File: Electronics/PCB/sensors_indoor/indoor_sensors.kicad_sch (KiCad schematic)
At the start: 11 parts, among them J3 B5B-ZR, U2 SHT45-AD1F, U3 SCD41-D-R2, U4 SGP41, U5 LPS22DF, U6 TSOP38436, U8 SPS30, U9 OPT4001DTSR

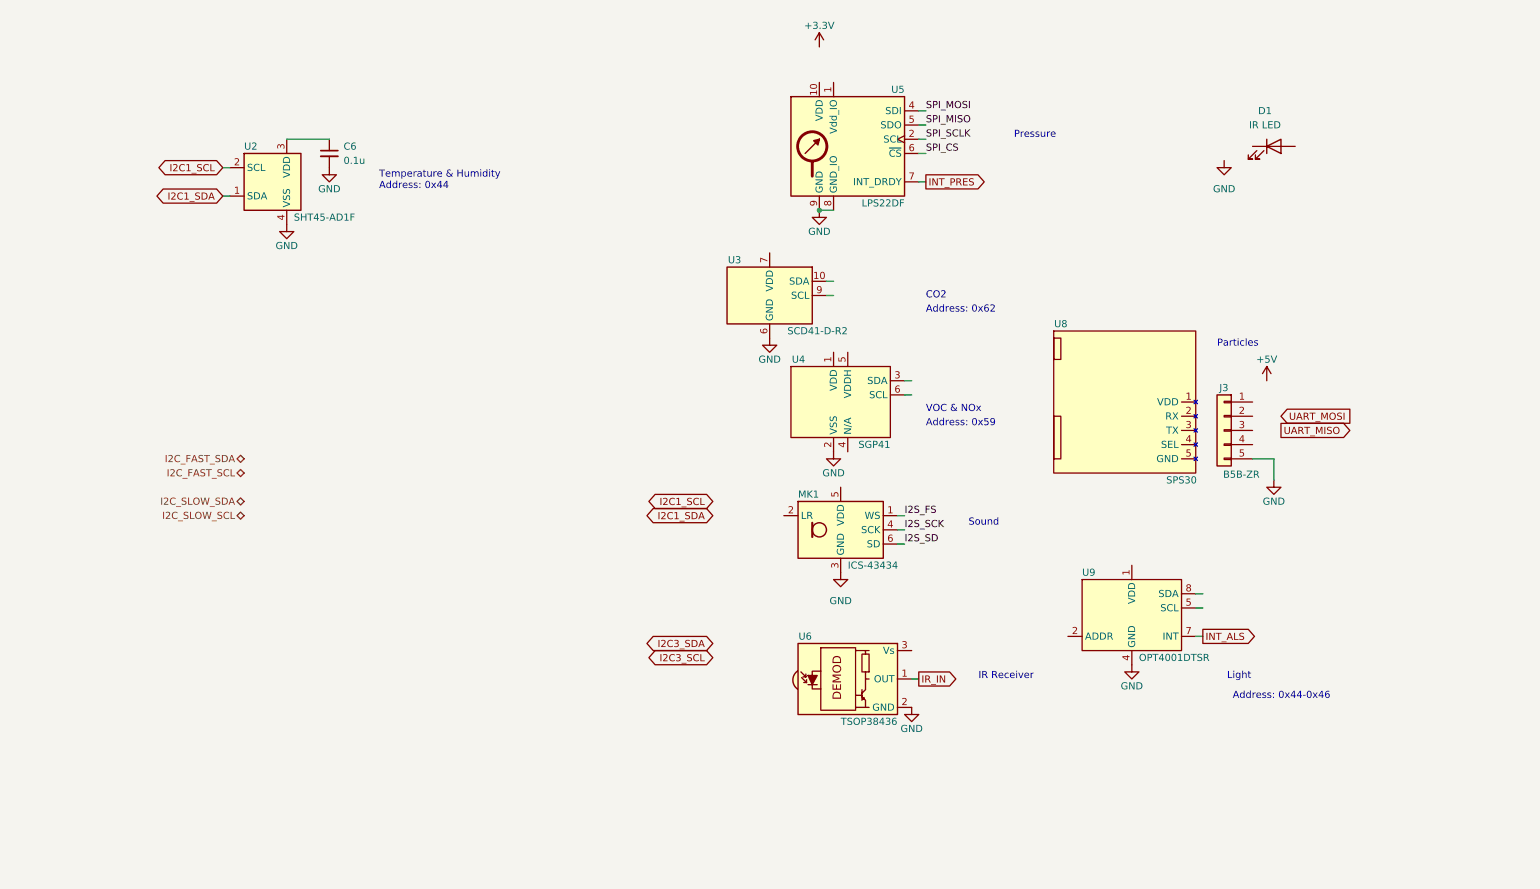
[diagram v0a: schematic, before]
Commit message: Added mounting holes and power supply
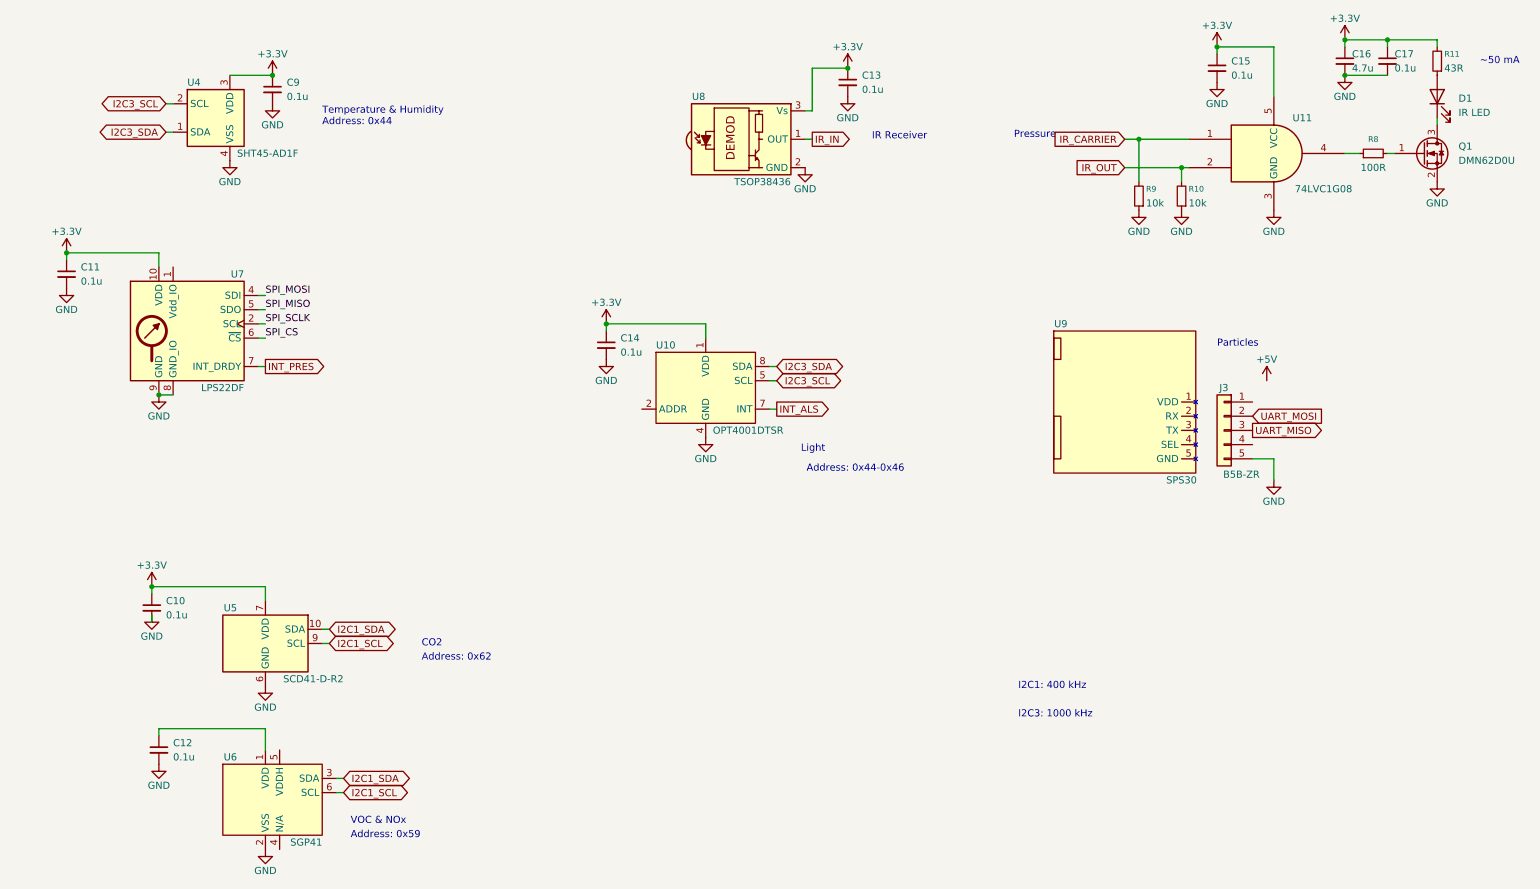
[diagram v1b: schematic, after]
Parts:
- removed MK1: ICS-43434, Sensor_Audio:InvenSense_ICS-43434-6_3.5x2.65mm, symbol Sensor_Audio:ICS-43434
- added C10, C11, C12, C13, C14, C15, C17: 0.1u, Capacitor_SMD:C_0402_1005Metric, symbol Device:C_Small
- added C16: 4.7u, Capacitor_SMD:C_0805_2012Metric, symbol Device:C_Small
- added Q1: DMN62D0U, Package_TO_SOT_SMD:SOT-23, symbol Transistor_FET:Q_NMOS_GSD
- added R10, R9: 10k, Resistor_SMD:R_0603_1608Metric, symbol Device:R_Small
- added R11: 43R, Resistor_SMD:R_0805_2012Metric, symbol Device:R_Small
- added R8: 100R, Resistor_SMD:R_0603_1608Metric, symbol Device:R_Small
- added U11: 74LVC1G08, Package_TO_SOT_SMD:SOT-23-5, symbol 74xGxx:74LVC1G08
- C9: renamed from C6; footprint (none) -> Capacitor_SMD:C_0402_1005Metric
- J3: MPN (none) -> B5B-ZR(LF)(SN); Mouser PN (none) -> 306-B5BZRLFSNP
- renumbered U9 to U10, U2 to U4, U3 to U5, U4 to U6, U5 to U7, U6 to U8, U8 to U9
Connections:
- net +3.3V: now also C9.1, U10.1 (VDD), U4.3 (VDD), U5.19 (VDD), U5.7 (VDD), U7.10 (VDD), U8.3 (Vs), C10.1, C11.1, C13.1, C14.1, C15.1, C16.1, C17.1, R11.2, U11.5 (VCC)
- net GND: now also C10.2, C11.2, C12.2, C13.2, C14.2, C15.2, C16.2, C17.2, Q1.2 (S), R10.1, R9.1, U11.3 (GND)
- net I2C1_SCL: now also U5.9 (SCL), U6.6 (SCL); no longer U4.2 (SCL)
- net I2C1_SDA: now also U5.10 (SDA), U6.3 (SDA); no longer U4.1 (SDA)
- net I2C3_SCL: now also U10.5 (SCL), U4.2 (SCL)
- net I2C3_SDA: now also U10.8 (SDA), U4.1 (SDA)
- net UART_MISO: now also J3.3 (Pin_3)
- net UART_MOSI: now also J3.2 (Pin_2)
- net at D1.1 (K): now also Q1.3 (D)
- net at D1.2 (A): now also R11.1
- net at U6.1 (VDD): now also C12.1
- new net: R8.1, U11.4
- new net: Q1.1 (G), R8.2
- new net IR_CARRIER: R9.2, U11.1
- new net IR_OUT: R10.2, U11.2
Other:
- note added: "I2C1: 400 kHz"
- note added: "I2C3: 1000 kHz"
- note added: "~50 mA"
- note removed: "Sound"
- moved on the sheet: C9, D1, U10, U4, U5, U6, U7, U8

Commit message: Swapped sides of everything and started routing
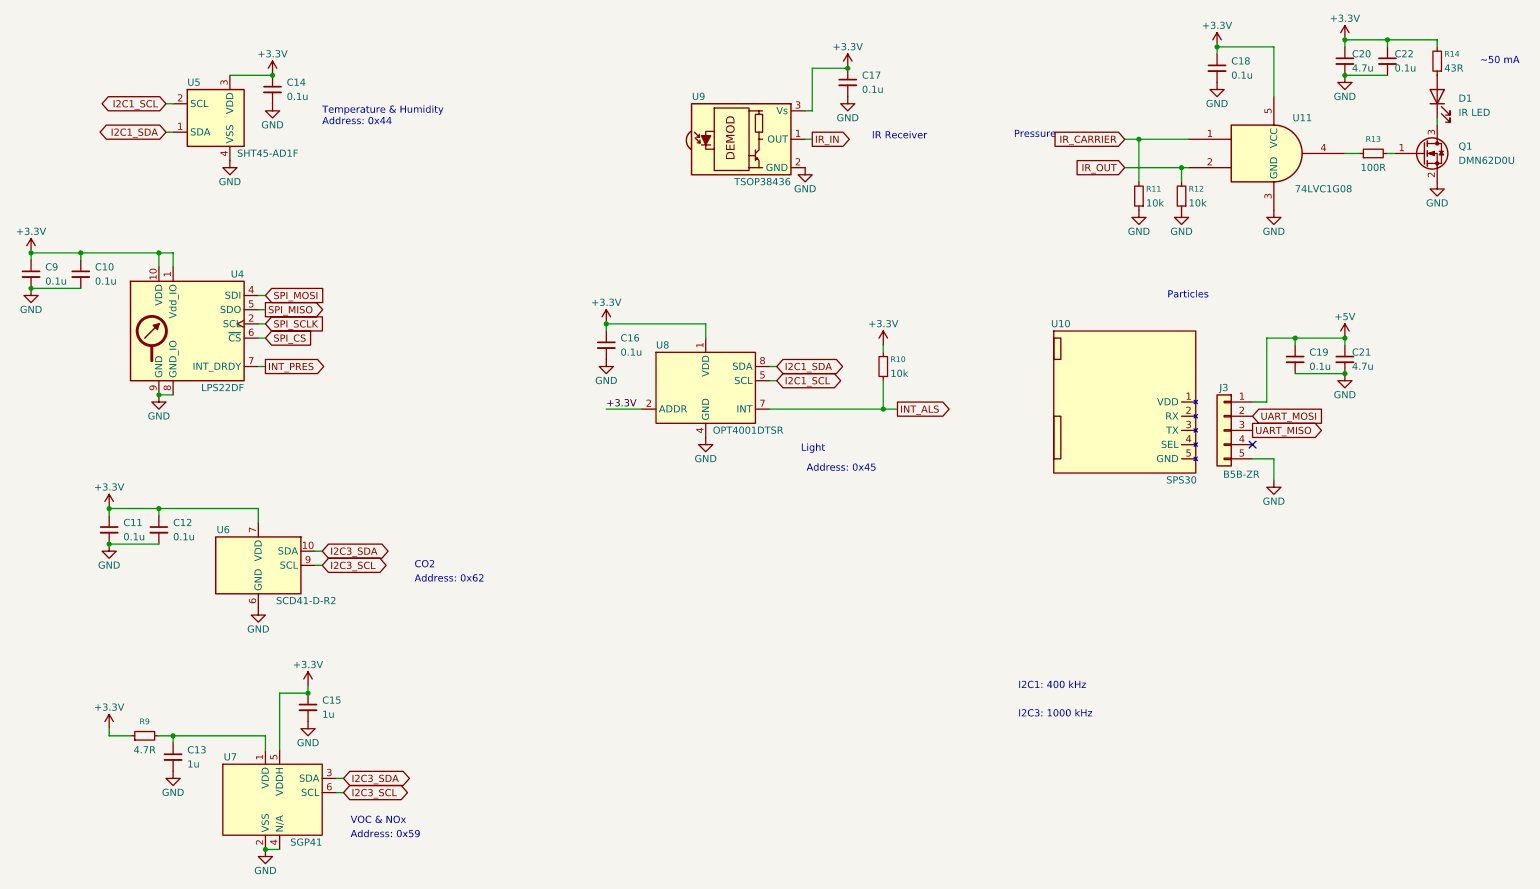
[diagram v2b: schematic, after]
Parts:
- added C10, C12, C19: 0.1u, Capacitor_SMD:C_0402_1005Metric, symbol Device:C_Small
- added C15: 1u, Capacitor_SMD:C_0402_1005Metric, symbol Device:C_Small
- added C21: 4.7u, Capacitor_SMD:C_0805_2012Metric, symbol Device:C_Small
- added R10: 10k, Resistor_SMD:R_0603_1608Metric, symbol Device:R_Small
- added R9: 4.7R, Resistor_SMD:R_0603_1608Metric, symbol Device:R_Small
- C13: renamed from C12; value 0.1u -> 1u
- renumbered C10 to C11, C9 to C14, C14 to C16, C13 to C17, C15 to C18, C16 to C20, C17 to C22, C11 to C9, R9 to R11, R10 to R12, R8 to R13, R11 to R14, U9 to U10, U7 to U4, U4 to U5, U5 to U6, U6 to U7, U10 to U8, U8 to U9
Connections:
- net +3.3V: now also U4.1 (Vdd_IO), U7.5 (VDDH), U8.2 (ADDR), C10.1, C12.1, C15.1, R10.2, R9.1
- net +5V: now also J3.1 (Pin_1), C19.1, C21.1
- net GND: now also U7.4 (N/A), C10.2, C12.2, C15.2, C19.2, C21.2
- net I2C1_SCL: now also U5.2 (SCL), U8.5 (SCL); no longer U6.9 (SCL), U7.6 (SCL)
- net I2C1_SDA: now also U5.1 (SDA), U8.8 (SDA); no longer U6.10 (SDA), U7.3 (SDA)
- net I2C3_SCL: now also U6.9 (SCL), U7.6 (SCL); no longer U5.2 (SCL), U8.5 (SCL)
- net I2C3_SDA: now also U6.10 (SDA), U7.3 (SDA); no longer U5.1 (SDA), U8.8 (SDA)
- net INT_ALS: now also R10.1
- net at C13.1, U7.1 (VDD): now also R9.2
- no-connect marks 0 -> 1
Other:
- note added: "Address: 0x45"
- note removed: "Address: 0x44-0x46"
- moved on the sheet: C11, C13, C9, U6

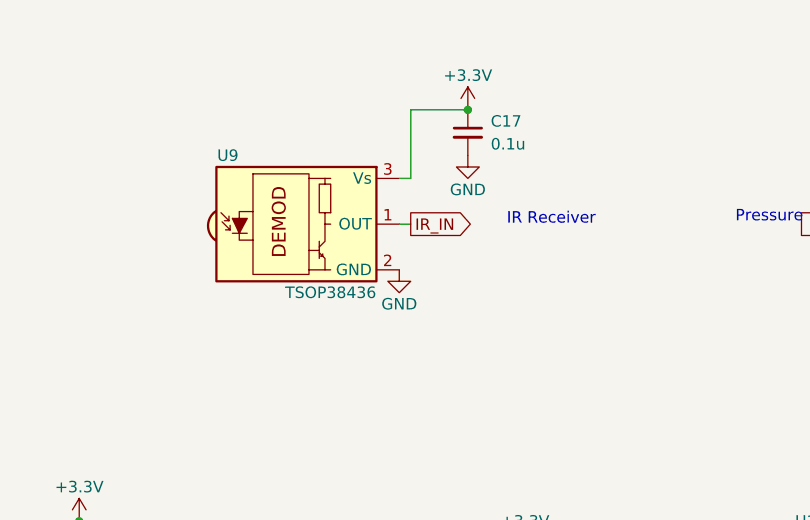
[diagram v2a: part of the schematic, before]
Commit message: Updated PCB with SMD IR tx/rx
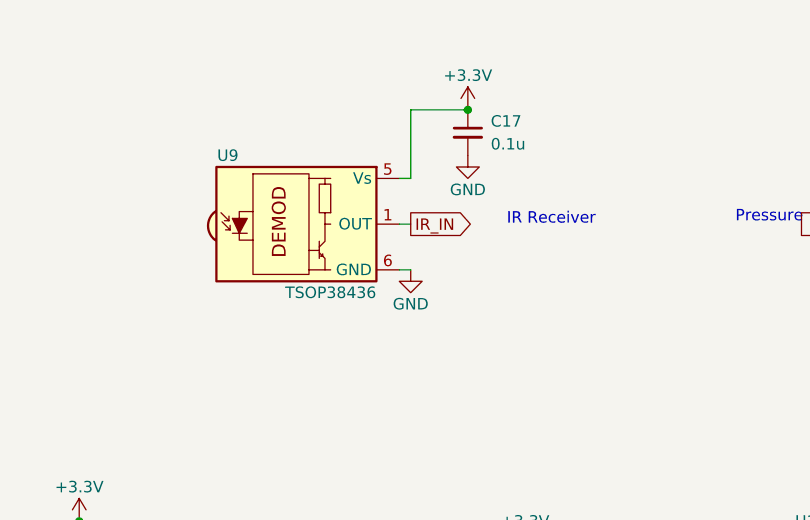
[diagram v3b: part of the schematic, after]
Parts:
- D1: footprint LED_THT:LED_D5.0mm_Clear -> DWlib:Osram_LED_SFH-4243
- U10: MPN (none) -> SPS30; Mouser PN (none) -> 403-SPS30
- U4: MPN (none) -> LPS22DFTR; Mouser PN (none) -> 511-LPS22DFTR
- U5: MPN (none) -> SHT45-AD1F-R2; Mouser PN (none) -> 403-SHT45-AD1F-R2
- U6: MPN (none) -> SCD41-D-R2; Mouser PN (none) -> 403-SCD41-D-R2
- U7: MPN (none) -> SGP41-D-R4; Mouser PN (none) -> 403-SGP41-D-R4
- U9: footprint OptoDevice:Vishay_MINICAST-3Pin -> DWlib:Vishay_BELOBOG-4Pin; symbol Interface_Optical:TSOP384xx -> DWlib:TSOP374xx; MPN (none) -> TSOP37436TT1; Mouser PN (none) -> 78-TSOP37436TT1
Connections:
- net +3.3V: now also U9.5 (Vs); no longer U9.3 (Vs)
- net GND: now also U9.6 (GND), U9.8 (GND); no longer U9.2 (GND)
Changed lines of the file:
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@@
 	(wire
 		(pts
+			(xy 156.21 48.26) (xy 154.94 48.26)
+		)
+		(stroke
+			(width 0)
+			(type default)
+		)
+	)
+	(wire
+		(pts
 			(xy 52.07 31.75) (xy 59.69 31.75)
 		)
@@
 			)
 		)
-		(property "Footprint" "LED_THT:LED_D5.0mm_Clear"
+		(property "Footprint" "DWlib:Osram_LED_SFH-4243"
 			(at 267.97 35.56 0)
 			(effects
@@
 			)
 		)
-		(property "MPN" ""
+		(property "MPN" "SCD41-D-R2"
 			(at 57.15 119.38 0)
 			(effects
@@
 			)
 		)
-		(property "Mouser PN" ""
+		(property "Mouser PN" "403-SCD41-D-R2"
 			(at 57.15 119.38 0)
 			(effects
@@
 			)
 		)
-		(property "MPN" ""
+		(property "MPN" "SGP41-D-R4"
 			(at 59.69 161.29 0)
 			(effects
@@
 			)
 		)
-		(property "Mouser PN" ""
+		(property "Mouser PN" "403-SGP41-D-R4"
 			(at 59.69 161.29 0)
 			(effects
@@
 	(symbol
 		(lib_id "power:GND")
-		(at 154.94 48.26 0)
+		(at 156.21 48.26 0)
 		(unit 1)
 		(exclude_from_sim no)
@@
 		(dnp no)
 		(property "Reference" "#PWR042"
-			(at 154.94 54.61 0)
+			(at 156.21 54.61 0)
 			(effects
 				(font
@@
 		)
 		(property "Value" "GND"
-			(at 154.94 52.07 0)
+			(at 156.21 52.07 0)
 			(effects
 				(font
@@
 		)
 		(property "Footprint" ""
-			(at 154.94 48.26 0)
+			(at 156.21 48.26 0)
 			(effects
 				(font
@@
 		)
 		(property "Datasheet" ""
-			(at 154.94 48.26 0)
+			(at 156.21 48.26 0)
 			(effects
 				(font
@@
 		)
 		(property "Description" "Power symbol creates a global label with name \"GND\" , ground"
-			(at 154.94 48.26 0)
+			(at 156.21 48.26 0)
 			(effects
 				(font
@@
 			)
 		)
-		(property "MPN" ""
+		(property "MPN" "LPS22DFTR"
 			(at 44.45 78.74 0)
 			(effects
@@
 			)
 		)
-		(property "Mouser PN" ""
+		(property "Mouser PN" "511-LPS22DFTR"
 			(at 44.45 78.74 0)
 			(effects
@@
 			)
 		)
-		(property "MPN" ""
+		(property "MPN" "SHT45-AD1F-R2"
 			(at 49.53 39.37 0)
 			(effects
@@
 			)
 		)
-		(property "Mouser PN" ""
+		(property "Mouser PN" "403-SHT45-AD1F-R2"
 			(at 49.53 39.37 0)
 			(effects
@@
 			)
 		)
-		(property "MPN" ""
+		(property "MPN" "SPS30"
 			(at 212.09 90.17 0)
 			(effects
@@
 			)
 		)
-		(property "Mouser PN" ""
+		(property "Mouser PN" "403-SPS30"
 			(at 212.09 90.17 0)
 			(effects
@@
 	)
 	(symbol
-		(lib_id "Interface_Optical:TSOP384xx")
+		(lib_id "DWlib:TSOP374xx")
 		(at 144.78 43.18 0)
 		(unit 1)
@@
 			)
 		)
-		(property "Footprint" "OptoDevice:Vishay_MINICAST-3Pin"
+		(property "Footprint" "DWlib:Vishay_BELOBOG-4Pin"
 			(at 143.51 52.705 0)
 			(effects
@@
 			)
 		)
-		(property "Datasheet" "http://www.vishay.com/docs/82491/tsop382.pdf"
+		(property "Datasheet" "https://www.vishay.com/docs/82599/tsop372.pdf"
 			(at 161.29 35.56 0)
 			(effects
@@
 			)
 		)
-		(property "MPN" ""
+		(property "MPN" "TSOP37436TT1"
 			(at 144.78 43.18 0)
 			(effects
@@
 			)
 		)
-		(property "Mouser PN" ""
+		(property "Mouser PN" "78-TSOP37436TT1"
 			(at 144.78 43.18 0)
 			(effects
@@
 			)
 		)
-		(pin "3"
+		(pin "6"
 		)
 		(pin "1"
 		)
-		(pin "2"
+		(pin "8"
+		)
+		(pin "5"
 		)
 		(instances
